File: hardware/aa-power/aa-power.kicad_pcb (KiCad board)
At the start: 4 copper layers, 175.3 x 96.5 mm, 172 parts, among them CN1 Barrel_Jack, CN10 6P6C, CN11 6P6C, CN12 6P6C, CN13 6P6C, CN14 Conn_01x08, CN15 Conn_01x08, CN16 Conn_01x08, CN17 8P8C, CN18 8P8C, CN19 8P8C, CN2 Conn_01x02, CN20 Conn_01x02, CN21 Conn_01x02, CN22 Conn_01x02, CN23 Conn_01x02, CN24 Conn_01x02, CN25 Conn_01x02, CN3 Conn_01x06, CN4 Conn_01x06, CN5 6P6C, CN6 Conn_01x04, CN7 Conn_01x04, CN8 Conn_01x04, CN9 Conn_01x04, Q1 TN1610H, U1 24LC08, U2 NIS5132xx, U3 uA7805, U4 75ALS192, U5 75ALS192, U6 75ALS192, U7 75ALS192, U8 75ALS192

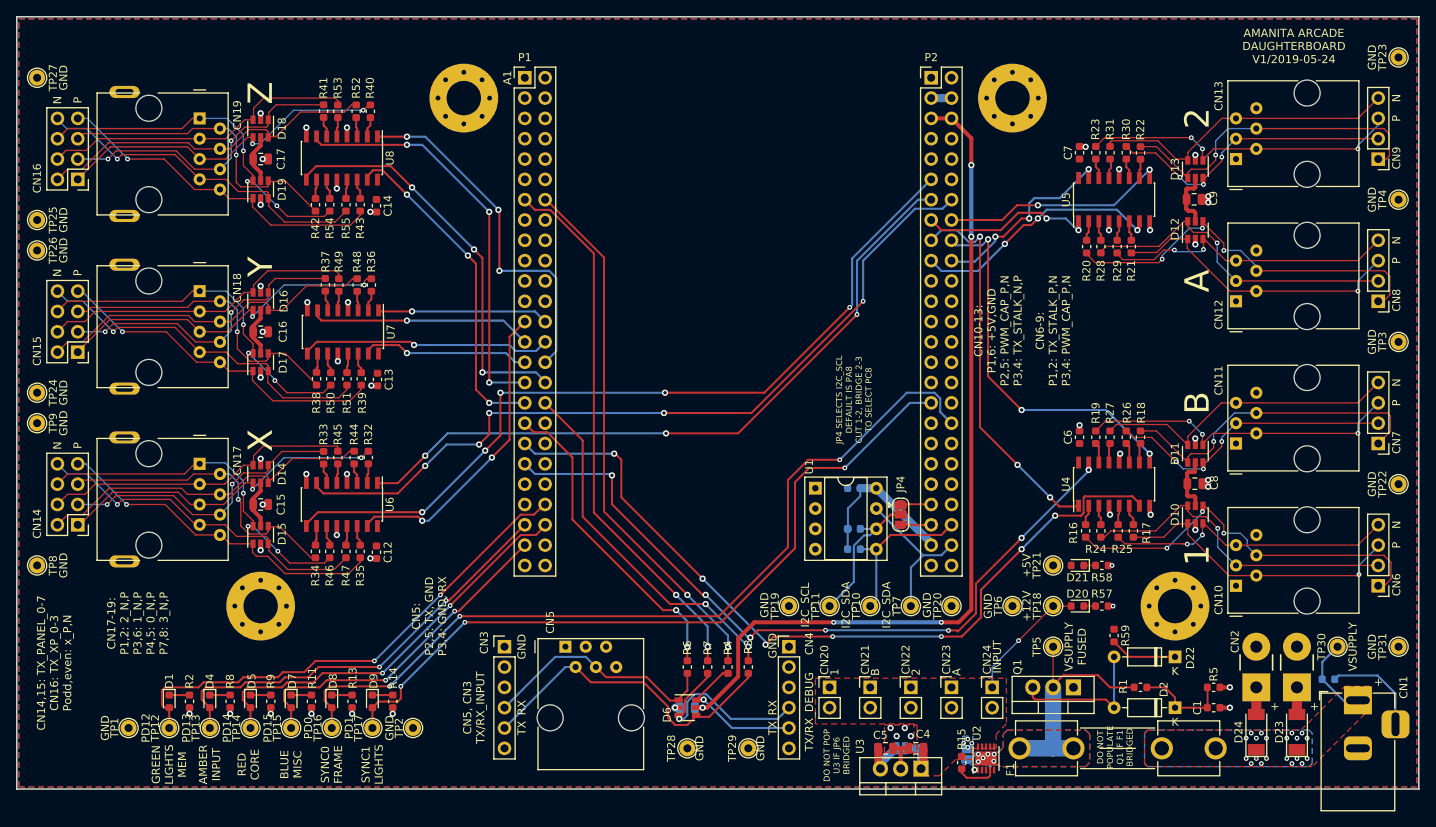
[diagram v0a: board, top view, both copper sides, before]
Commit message: Design, lay out power protection/distribution board
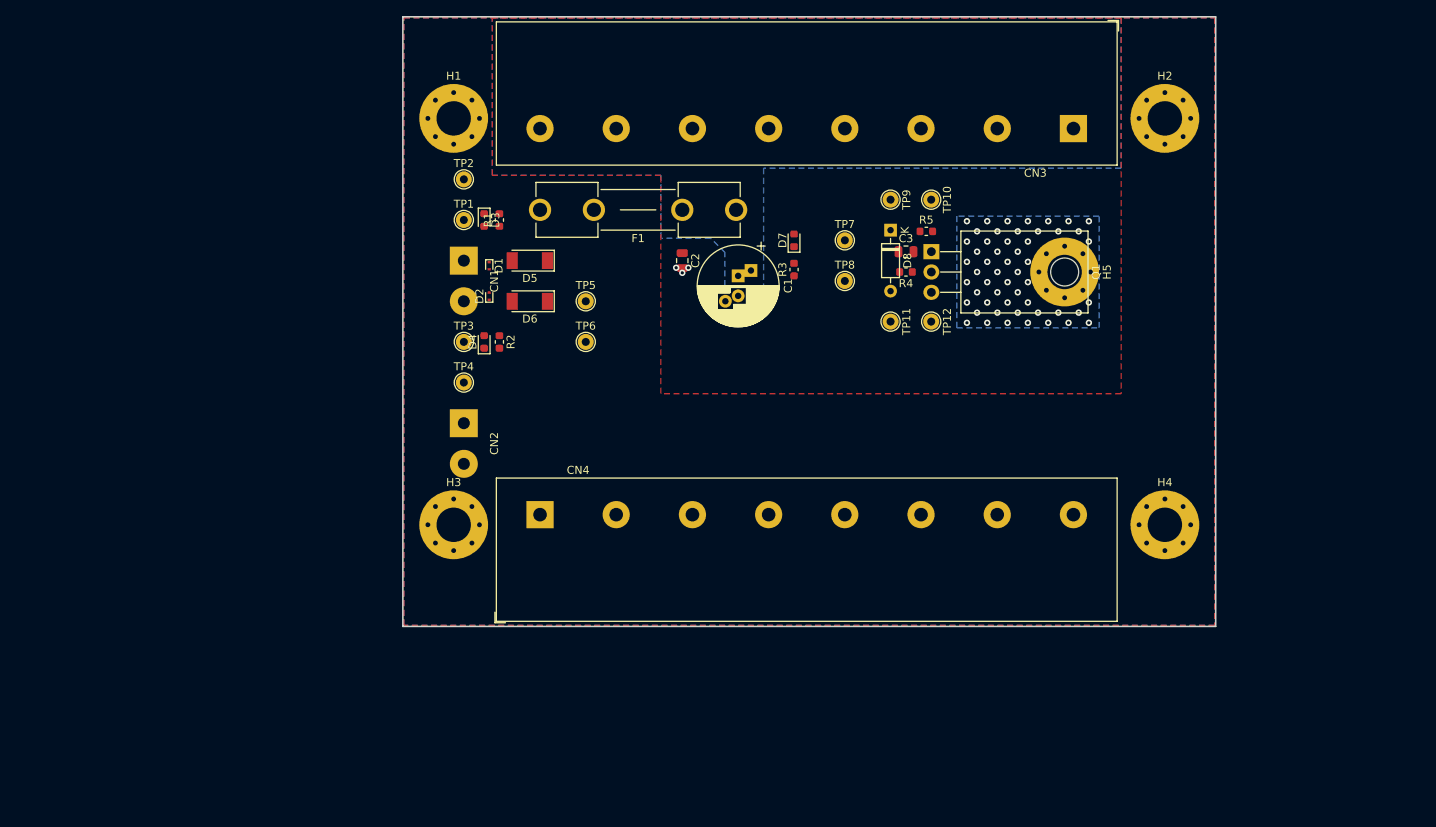
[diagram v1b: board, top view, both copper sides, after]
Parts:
- removed A1: STM32F407_Discovery_P1_P2, aa-power:STM32F407_Discovery_P1_P2_Socket
- removed C12, C13, C14, C6, C7: 0.1u, Capacitor_SMD:C_0603_1608Metric
- removed C15, C16, C17, C8, C9: 1u, Capacitor_SMD:C_0805_2012Metric
- removed C4, C5: 10u, Capacitor_SMD:C_0805_2012Metric
- removed CN10, CN11, CN12, CN13, CN5: 6P6C, aa-power:6P6C_Assmann_A-2014-1-4
- removed CN14, CN15, CN16: Conn_01x08, Connector_PinHeader_2.54mm:PinHeader_2x04_P2.54mm_Vertical
- removed CN17, CN18, CN19: 8P8C, aa-power:8P8C_Assmann_A-2014-2S-4
- removed CN20, CN21, CN22, CN23, CN24: Conn_01x02, Connector_PinHeader_2.54mm:PinHeader_1x02_P2.54mm_Vertical
- removed CN25: Conn_01x02, Connector_Wire:SolderWirePad_1x02_P5.08mm_Drill1.5mm
- removed CN6, CN7, CN8, CN9: Conn_01x04, Connector_PinHeader_2.54mm:PinHeader_1x04_P2.54mm_Vertical
- removed D10, D11, D12, D13, D14, D15, D16, D17, D18, D19: D5V0P4UR6SO, Package_TO_SOT_SMD:SOT-23-6
- removed D20, D21, D9: LED, LED_SMD:LED_0603_1608Metric
- removed D22: BZX79C5V1, Diode_THT:D_DO-35_SOD27_P7.62mm_Horizontal
- removed D23, D24: D_Schottky, aa-power:D_SOD-128
- removed JP4: SolderJumper_3_Bridged12, Jumper:SolderJumper-3_P1.3mm_Bridged2Bar12_RoundedPad1.0x1.5mm
- removed JP5, JP7: SolderJumper_2_Open, Jumper:SolderJumper-2_P1.3mm_Open_RoundedPad1.0x1.5mm
- removed R10, R12, R56: 10k, Resistor_SMD:R_0603_1608Metric
- removed R11, R13, R14, R59, R8, R9: 220, Resistor_SMD:R_0603_1608Metric
- removed R15: 33, Resistor_SMD:R_0603_1608Metric
- removed R16, R17, R18, R19, R20, R21, R22, R23, R24, R25, R26, R27, R28, R29, R30, R31, R32, R33, R34, R35, R36, R37, R38, R39, R40, R41, R42, R43, R44, R45, R46, R47, R48, R49, R50, R51, R52, R53, R54, R55: 56, Resistor_SMD:R_0603_1608Metric
- removed R57: 2.2k, Resistor_SMD:R_0603_1608Metric
- removed R58: 680, Resistor_SMD:R_0603_1608Metric
- removed R6, R7: 1k, Resistor_SMD:R_0603_1608Metric
- removed TP13, TP14, TP15, TP16, TP17, TP18, TP19, TP20, TP21, TP22, TP23, TP24, TP25, TP26, TP27, TP28, TP29, TP30, TP31: TestPoint, TestPoint:TestPoint_THTPad_D2.0mm_Drill1.0mm
- removed U1: 24LC08, Package_DIP:DIP-8_W7.62mm_Socket
- removed U2: NIS5132xx, Package_DFN_QFN:DFN-10-1EP_3x3mm_P0.5mm_EP1.75x2.7mm
- removed U3: uA7805, Package_TO_SOT_THT:TO-220-3_Vertical
- removed U4, U5, U6, U7, U8: 75ALS192, Package_SO:SOIC-16_3.9x9.9mm_P1.27mm
- added H5: MountingHole_Pad, MountingHole:MountingHole_4.3mm_M4_Pad_Via, F.Cu at (184.3, 82.7)
- C1: value 10n -> 100u; footprint Capacitor_SMD:C_0603_1608Metric -> Capacitor_THT:CP_Radial_D10.0mm_P2.50mm_P5.00mm
- C2: moved to F.Cu
- C3: value 0.1u -> 1u; footprint Capacitor_SMD:C_0603_1608Metric -> Capacitor_SMD:C_0805_2012Metric; moved to F.Cu
- CN1: value Barrel_Jack -> 12V_IN; footprint Connector_BarrelJack:BarrelJack_Horizontal -> Connector_Wire:SolderWirePad_1x02_P5.08mm_Drill1.5mm
- CN2: value Conn_01x02 -> GND_IN
- CN3: value Conn_01x06 -> 12V_OUT; footprint Connector_PinHeader_2.54mm:PinHeader_1x06_P2.54mm_Vertical -> aa-shared:TerminalBlock_OST_OSTYK44108030
- CN4: value Conn_01x06 -> GND_OUT; footprint Connector_PinHeader_2.54mm:PinHeader_1x06_P2.54mm_Vertical -> aa-shared:TerminalBlock_OST_OSTYK44108030
- D1: value LED -> DF2S16FS; footprint LED_SMD:LED_0603_1608Metric -> aa-shared:D_SOD-923
- D2: value BZX79C15 -> DF2S16FS; footprint Diode_THT:D_DO-35_SOD27_P7.62mm_Horizontal -> aa-shared:D_SOD-923
- D3: value DF2S16FS -> LED; footprint aa-power:D_SOD-923 -> LED_SMD:LED_0603_1608Metric; moved to F.Cu
- D5: value LED -> D_Schottky; footprint LED_SMD:LED_0603_1608Metric -> aa-shared:D_SOD-128
- D6: value D5V0P4UR6SO -> D_Schottky; footprint Package_TO_SOT_SMD:SOT-23-6 -> aa-shared:D_SOD-128
- D8: value LED -> BZX79C15; footprint LED_SMD:LED_0603_1608Metric -> Diode_THT:D_DO-35_SOD27_P7.62mm_Horizontal
- F1: footprint aa-power:Fuseholder_Clip_5x20_Bel_FC-211-22 -> aa-shared:Fuseholder_Clip_5x20_Bel_FC-211-22
- Q1: footprint Package_TO_SOT_THT:TO-220-3_Vertical -> Package_TO_SOT_THT:TO-220-3_Horizontal_TabDown
- R1, R2: value 220 -> 2.2k
- R3: value 120 -> 2.2k
- R4: value 120 -> 470
- TP1: value TestPoint -> 12V_IN_A
- TP10, TP12, TP2, TP4, TP5, TP6, TP8: value TestPoint -> GND
- TP11: value TestPoint -> 12V_IN
- TP3: value TestPoint -> 12V_IN_B
- moved CN1 124.5 mm to (109.2, 81.3), turned to 270 degrees
- moved TP4 119.1 mm to (109.2, 96.5), turned to 0 degrees
- moved TP3 116.8 mm to (109.2, 91.4), turned to 0 degrees
- moved TP9 110.3 mm to (162.6, 73.7)
- moved TP12 107.9 mm to (167.6, 88.9), turned to 270 degrees
- moved TP8 107.0 mm to (156.8, 83.8), turned to 0 degrees
- moved CN2 104.4 mm to (109.2, 101.6), turned to 270 degrees
- moved D2 100.0 mm to (112.4, 85.7), turned to 90 degrees
- moved R1 99.2 mm to (113.7, 76.2), turned to 90 degrees
- moved CN3 96.2 mm to (185.4, 64.8), turned to 180 degrees
- moved D3 92.7 mm to (111.8, 76.2)
- moved D8 91.4 mm to (162.6, 77.5)
- moved H3 90.7 mm to (108.0, 114.3), turned to 0 degrees
- moved H2 87.7 mm to (196.8, 63.5), turned to 0 degrees
- moved D7 85.3 mm to (150.5, 78.7), turned to 90 degrees
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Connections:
- C1 pad 1: Net-(C1-Pad1) -> /Q1_TAB
- C2 pad 1: +3V -> /Q1_TAB
- C3 pad 1: /MEM_PWR -> Net-(C3-Pad1)
- CN1 pad 2: GND -> Net-(CN1-Pad2)
- CN2 pad 1: Net-(CN2-Pad1) -> GND
- CN3 pad 1: GND -> /Q1_TAB
- CN3 pad 2: Net-(CN3-Pad2) -> /Q1_TAB
- CN3 pad 3: Net-(CN3-Pad3) -> /Q1_TAB
- CN3 pad 4: /RX_INPUT_S -> /Q1_TAB
- CN3 pad 5: /TX_INPUT_S -> /Q1_TAB
- CN3 pad 6: Net-(CN3-Pad6) -> /Q1_TAB
- CN4 pad 2: Net-(CN4-Pad2) -> GND
- CN4 pad 3: Net-(CN4-Pad3) -> GND
- CN4 pad 4: /RX_DEBUG_S -> GND
- CN4 pad 5: /TX_DEBUG_S -> GND
- CN4 pad 6: Net-(CN4-Pad6) -> GND
- D1 pad 1: Net-(D1-Pad1) -> Net-(CN1-Pad1)
- D1 pad 2: /DB_GREEN -> GND
- D2 pad 1: Net-(C1-Pad1) -> Net-(CN1-Pad2)
- D2 pad 2: Net-(D2-Pad2) -> GND
- D3 pad 2: GND -> Net-(CN1-Pad1)
- D4 pad 2: /DB_ORANGE -> Net-(CN1-Pad2)
- D5 pad 2: /DB_RED -> Net-(CN1-Pad1)
- D6 pad 1: /RX_INPUT_S -> Net-(D5-Pad1)
- D6 pad 2: GND -> Net-(CN1-Pad2)
- D7 pad 2: /DB_BLUE -> /Q1_TAB
- D8 pad 1: Net-(D8-Pad1) -> Net-(C3-Pad1)
- D8 pad 2: /DB_SYNC_0 -> Net-(D8-Pad2)
- F1 pad 1: Net-(D3-Pad1) -> /Q1_TAB
- F1 pad 2: Net-(CN1-Pad1) -> Net-(D5-Pad1)
- Q1 pad 2: Net-(D3-Pad1) -> /Q1_TAB
- Q1 pad 3: Net-(D2-Pad2) -> Net-(D8-Pad2)
- R1 pad 1: Net-(D3-Pad1) -> GND
- R1 pad 2: Net-(C1-Pad1) -> Net-(D3-Pad1)
- R2 pad 2: Net-(D1-Pad1) -> Net-(D4-Pad1)
- R3 pad 1: /TX_INPUT -> GND
- R3 pad 2: /TX_INPUT_S -> Net-(D7-Pad1)
- R4 pad 1: /TX_DEBUG -> /Q1_TAB
- R4 pad 2: /TX_DEBUG_S -> Net-(C3-Pad1)
- R5 pad 1: Net-(C1-Pad1) -> Net-(C3-Pad1)
- TP1 pad 1: GND -> Net-(CN1-Pad1)
- TP10 pad 1: /I2C_SDA -> GND
- TP11 pad 1: /I2C_SCL -> Net-(D8-Pad2)
- TP12 pad 1: /DB_GREEN -> GND
- TP3 pad 1: GND -> Net-(CN1-Pad2)
- TP5 pad 1: Net-(D3-Pad1) -> Net-(D5-Pad1)
- TP7 pad 1: /MEM_WP -> /Q1_TAB
- TP9 pad 1: GND -> Net-(C3-Pad1)
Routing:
- net +3V: track 108.1 -> 0.00 mm, vias 5 -> 0
- net /DB_SYNC_0: track 106.4 -> 0.00 mm, vias 3 -> 0
- net /TX_PANEL_2: track 103.1 -> 0.00 mm, vias 5 -> 0
- net /PWM_CAP_1: track 101.7 -> 0.00 mm, vias 7 -> 0
- net /TX_PANEL_1: track 99.9 -> 0.00 mm, vias 5 -> 0
- net /DB_SYNC_1: track 93.9 -> 0.00 mm, vias 3 -> 0
- net /PWM_CAP_B: track 93.5 -> 0.00 mm, vias 7 -> 0
- net /TX_PANEL_0: track 88.0 -> 0.00 mm, vias 3 -> 0
- net /RX_DEBUG: track 68.2 -> 0.00 mm, vias 2 -> 0
- net /TX_DEBUG: track 67.2 -> 0.00 mm, vias 2 -> 0
- net /DB_GREEN: track 63.0 -> 0.00 mm, vias 2 -> 0
- net /DB_ORANGE: track 54.5 -> 0.00 mm, vias 2 -> 0
- net /TX_XP_1: track 51.5 -> 0.00 mm, vias 3 -> 0
- net /DB_RED: track 51.5 -> 0.00 mm, vias 2 -> 0
- net /TX_XP_2: track 50.3 -> 0.00 mm, vias 3 -> 0
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- added copper zone on B.Cu, net /Q1_TAB
- added copper zone on F.Cu, net /Q1_TAB
- removed copper zone on F.Cu, net +5V
- removed copper zone on B.Cu, net Net-(CN1-Pad1)
- removed copper zone on F.Cu, net Net-(CN1-Pad1)
- removed copper zone on B.Cu, net Net-(D3-Pad1)
- removed copper zone on F.Cu, net Net-(D3-Pad1)
- removed copper zone on B.Cu, net VDD
- removed copper zone on F.Cu, net VDD
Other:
- board size 175.3 x 96.5 mm -> 101.6 x 76.2 mm
- copper layers 4 -> 2
- net class Default: clearance 0.1524 -> 0.254; via_dia 0.7874 -> 0.8; via_drill 0.4064 -> 0.4
- net class High Current removed
- net class Line Drive Broadside removed
- net class Line Drive Microstrip removed
- net class Power removed
- rule pad_to_mask_clearance: 0.051 -> 0
- rule trace_clearance: 0.1524 -> 0.254
- board text removed: "+"
- board text removed: "+12V"
- board text removed: "+5V"
- board text removed: "1"
- board text removed: "2"
- board text removed: "A"
- board text removed: "AMANITA ARCADE DAUGHTERBOARD V1/2019-05-24"
- board text removed: "AMBER INPUT"
- board text removed: "B"
- board text removed: "BLUE MISC"
- board text removed: "BRIDGE JP5 IF U2 NOT POPULATED"
- board text removed: "BRIDGE JP6 TO USE +5V FROM STM32F4 DISCOVERY BOARD A1 DO NOT POPULATE U3"
- board text removed: "BRIDGE JP7 TO CONNECT VDD AND +5V POWER INPUT MUST BE REGULATED DO NOT POPULATE U3"
- board text removed: "CN10-13: P1,6: +5V,GND P2,5: PWM_CAP_P,N P3,4: TX_STALK_N,P"
- board text removed: "CN14,15: TX_PANEL_0-7 CN16: TX_XP_0-3 Podd,even: x_P,N"
- board text removed: "CN17-19: P1,2: 2_N,P P3,6: 1_N,P P4,5: 0_N,P P7,8: 3_N,P"
- board text removed: "CN5, CN3 TX/RX_INPUT"
- board text removed: "CN5: P2,5: TX, GND P3,4: GND, RX"
- board text removed: "CN6-9: P1,2: TX_STALK_P,N P3,4: PWM_CAP_P,N"
- board text removed: "CUT JP1 IF STM32F4 DISCOVERY BOARD A1 IS INDEPENDENTLY POWERED"
- board text removed: "DO NOT POP U3 IF JP6 BRIDGED"
- board text removed: "DO NOT POPULATE Q1 IF F1 BRIDGED"
- board text removed: "GND"
- board text removed: "GREEN LIGHTS MEM"
- board text removed: "I2C_SCL"
- board text removed: "I2C_SDA"
- board text removed: "INPUT"
- board text removed: "JP4 SELECTS I2C_SCL DEFAULT IS PA8 CUT 1-2, BRIDGE 2-3 TO SELECT PC8"
- board text removed: "N"
- board text removed: "P"
- board text removed: "PD0"
- board text removed: "PD1"
- board text removed: "PD12"
- board text removed: "PD13"
- board text removed: "PD14"
- board text removed: "PD15"
- board text removed: "R56 CONNECTS VSUPPLY AND GND WHEN CN1 UNPLUGGED"
- board text removed: "RED CORE"
- board text removed: "RX"
- board text removed: "SYNC0 FRAME"
- board text removed: "SYNC1 LIGHTS"
- board text removed: "TX"
- board text removed: "TX/RX_DEBUG"
- board text removed: "VSUPPLY"
- board text removed: "VSUPPLY FUSED"
- board text removed: "X"
- board text removed: "Y"
- board text removed: "Z"

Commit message: Substantial rework of system, new layouts done for daughterboard, power, stalk receiver
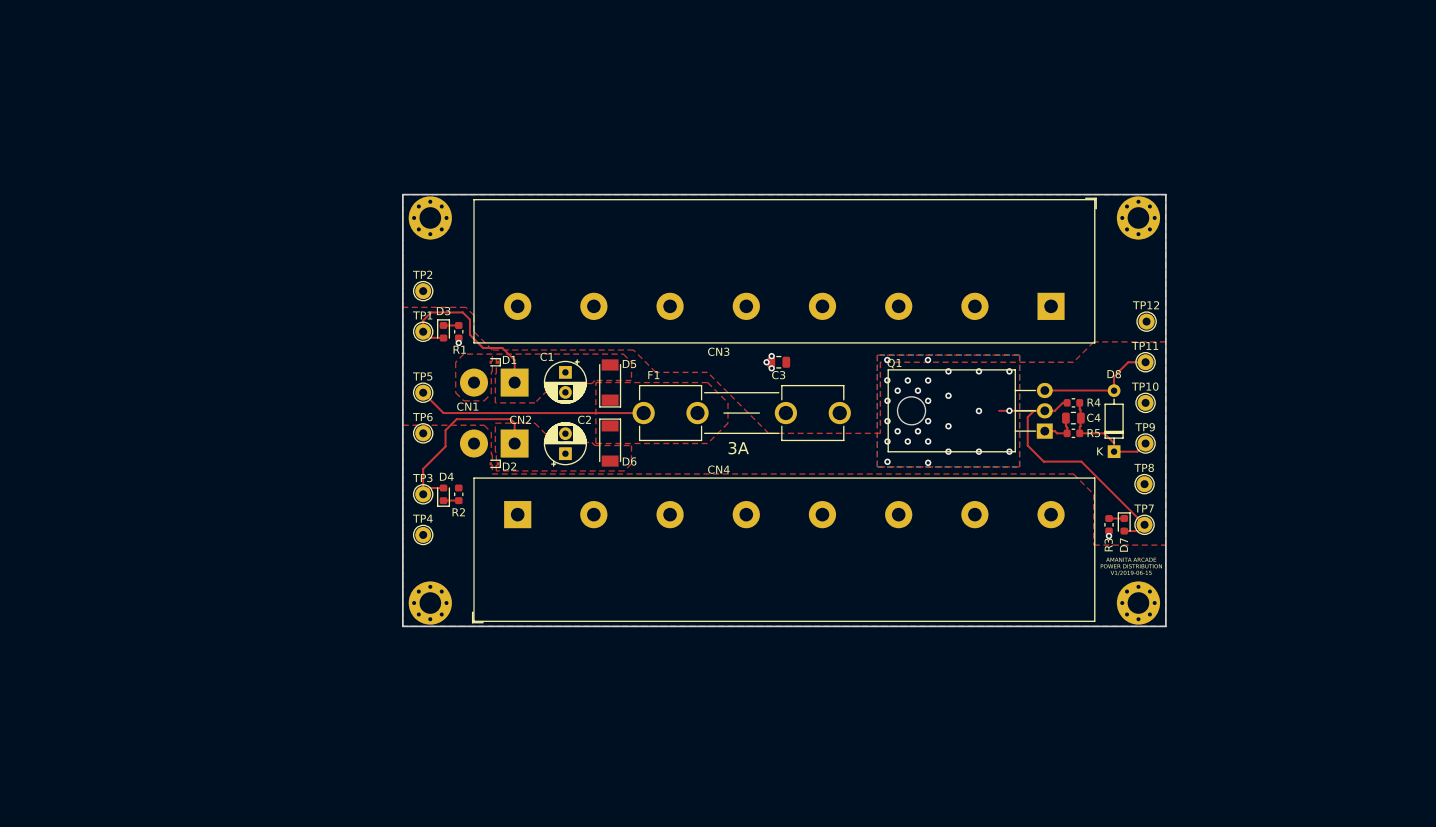
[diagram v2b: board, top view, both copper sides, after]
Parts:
- removed H5: MountingHole_Pad, MountingHole:MountingHole_4.3mm_M4_Pad_Via
- added C4: 1u, Capacitor_SMD:C_0805_2012Metric, F.Cu at (185.4, 101.0)
- C1: value 100u -> 10u; footprint Capacitor_THT:CP_Radial_D10.0mm_P2.50mm_P5.00mm -> Capacitor_THT:CP_Radial_D5.0mm_P2.50mm
- C2: value 1u -> 10u; footprint Capacitor_SMD:C_0805_2012Metric -> Capacitor_THT:CP_Radial_D5.0mm_P2.50mm
- CN1: value 12V_IN -> VIN_A
- CN2: value GND_IN -> VIN_B
- H1, H2, H3, H4: footprint MountingHole:MountingHole_4.3mm_M4_Pad_Via -> MountingHole:MountingHole_2.7mm_M2.5_Pad_Via
- moved H2 92.7 mm to (105.0, 75.9)
- moved H1 86.5 mm to (193.5, 75.9)
- moved D7 54.5 mm to (191.8, 114.3), turned to 270 degrees
- moved TP7 51.7 mm to (194.3, 114.3)
- moved R3 50.7 mm to (189.9, 114.3)
- moved TP8 45.3 mm to (194.3, 109.2)
- moved TP9 44.1 mm to (194.4, 104.1), turned to 0 degrees
- moved D8 39.3 mm to (190.5, 105.2), turned to 90 degrees
- moved TP10 36.9 mm to (194.4, 99.1), turned to 0 degrees
- moved TP11 32.3 mm to (194.4, 94.0), turned to 0 degrees
- moved R5 31.2 mm to (185.4, 102.9), turned to 180 degrees
- moved F1 28.5 mm to (156.2, 100.3)
- moved C2 28.2 mm to (121.9, 105.4), turned to 90 degrees
- moved TP12 26.9 mm to (194.6, 88.9), turned to 0 degrees
- moved R4 26.6 mm to (185.4, 99.1), turned to 0 degrees
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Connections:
- C1 pad 1: /Q1_TAB -> Net-(C1-Pad1)
- C2 pad 1: /Q1_TAB -> Net-(C2-Pad1)
- C3 pad 1: Net-(C3-Pad1) -> /+12V
- CN1 pad 1: Net-(CN1-Pad1) -> Net-(C1-Pad1)
- CN1 pad 2: Net-(CN1-Pad2) -> GND
- CN2 pad 1: GND -> Net-(C2-Pad1)
- CN3 pad 1: /Q1_TAB -> /+12V
- CN3 pad 2: /Q1_TAB -> /+12V
- CN3 pad 3: /Q1_TAB -> /+12V
- CN3 pad 4: /Q1_TAB -> /+12V
- CN3 pad 5: /Q1_TAB -> /+12V
- CN3 pad 6: /Q1_TAB -> /+12V
- CN3 pad 7: /Q1_TAB -> /+12V
- CN3 pad 8: /Q1_TAB -> /+12V
- D1 pad 1: Net-(CN1-Pad1) -> Net-(C1-Pad1)
- D2 pad 1: Net-(CN1-Pad2) -> Net-(C2-Pad1)
- D3 pad 2: Net-(CN1-Pad1) -> Net-(C1-Pad1)
- D4 pad 2: Net-(CN1-Pad2) -> Net-(C2-Pad1)
- D5 pad 2: Net-(CN1-Pad1) -> Net-(C1-Pad1)
- D6 pad 2: Net-(CN1-Pad2) -> Net-(C2-Pad1)
- D7 pad 2: /Q1_TAB -> /+12V
- D8 pad 1: Net-(C3-Pad1) -> Net-(C4-Pad1)
- F1 pad 1: /Q1_TAB -> /+12V
- Q1 pad 2: /Q1_TAB -> /+12V
- R4 pad 1: /Q1_TAB -> /+12V
- R4 pad 2: Net-(C3-Pad1) -> Net-(C4-Pad1)
- R5 pad 1: Net-(C3-Pad1) -> Net-(C4-Pad1)
- TP1 pad 1: Net-(CN1-Pad1) -> Net-(C1-Pad1)
- TP3 pad 1: Net-(CN1-Pad2) -> Net-(C2-Pad1)
- TP7 pad 1: /Q1_TAB -> /+12V
- TP9 pad 1: Net-(C3-Pad1) -> Net-(C4-Pad1)
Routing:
- net /+12V: track 0.00 -> 36.4 mm, vias 0 -> 28
- net Net-(D5-Pad1): track 0.00 -> 28.6 mm
- net Net-(C2-Pad1): track 0.00 -> 24.0 mm
- net Net-(C1-Pad1): track 0.00 -> 22.6 mm
- net Net-(D8-Pad2): track 0.00 -> 15.1 mm
- net Net-(C4-Pad1): track 0.00 -> 14.1 mm
- net GND: track 2.15 -> 8.28 mm, vias 3 -> 5
- net Net-(D7-Pad1): track 0.00 -> 2.04 mm
- net Net-(D4-Pad1): track 0.00 -> 1.92 mm
- net Net-(D3-Pad1): track 0.00 -> 1.92 mm
- net /Q1_TAB: vias 53 -> 0
- added copper zone on B.Cu, net /+12V
- added copper zone on F.Cu, net /+12V
- added copper zone on F.Cu, net Net-(C1-Pad1)
- added copper zone on F.Cu, net Net-(C2-Pad1)
- added copper zone on F.Cu, net Net-(D5-Pad1)
- removed copper zone on B.Cu, net /Q1_TAB
- removed copper zone on F.Cu, net /Q1_TAB
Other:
- board size 101.6 x 76.2 mm -> 95.4 x 54 mm
- board text added: "3A"
- board text added: "AMANITA ARCADE POWER DISTRIBUTION V1/2019-06-15"

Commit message: Final designs and actual sent gerbers for first for-real run
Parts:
- added FD1: Fiducial, Fiducial:Fiducial_1mm_Dia_2.54mm_Outer_CopperTop, F.Cu at (106.7, 119.4)
- added FD2: Fiducial, Fiducial:Fiducial_1mm_Dia_2.54mm_Outer_CopperTop, F.Cu at (191.8, 81.3)
- added FD5: Fiducial, aa-shared:StencilAlignment_1.27mm, F.Cu at (104.1, 119.4)
- added FD6: Fiducial, aa-shared:StencilAlignment_1.27mm, F.Cu at (194.3, 81.3)
- D5, D6: value D_Schottky -> TSS83L45
- D8: footprint Diode_THT:D_DO-35_SOD27_P7.62mm_Horizontal -> Diode_THT:D_DO-35_SOD27_P2.54mm_Vertical_KathodeUp
- TP1: value 12V_IN_A -> +12V_IN_A; footprint TestPoint:TestPoint_THTPad_D2.0mm_Drill1.0mm -> aa-shared:TestPoint_Loop_D1.80mm_Drill1.0mm_Beaded
- TP10, TP12, TP2, TP4, TP6, TP8: footprint TestPoint:TestPoint_THTPad_D2.0mm_Drill1.0mm -> aa-shared:TestPoint_Loop_D1.80mm_Drill1.0mm_Beaded
- TP11: value 12V_IN -> OV_TRIG; footprint TestPoint:TestPoint_THTPad_D2.0mm_Drill1.0mm -> aa-shared:TestPoint_Loop_D1.80mm_Drill1.0mm_Beaded
- TP3: value 12V_IN_B -> +12V_IN_B; footprint TestPoint:TestPoint_THTPad_D2.0mm_Drill1.0mm -> aa-shared:TestPoint_Loop_D1.80mm_Drill1.0mm_Beaded
- TP5: value GND -> +12V_UNFS; footprint TestPoint:TestPoint_THTPad_D2.0mm_Drill1.0mm -> aa-shared:TestPoint_Loop_D1.80mm_Drill1.0mm_Beaded
- TP7: value TestPoint -> +12V; footprint TestPoint:TestPoint_THTPad_D2.0mm_Drill1.0mm -> aa-shared:TestPoint_Loop_D1.80mm_Drill1.0mm_Beaded
- TP9: value TestPoint -> OV_Z; footprint TestPoint:TestPoint_THTPad_D2.0mm_Drill1.0mm -> aa-shared:TestPoint_Loop_D1.80mm_Drill1.0mm_Beaded
- moved D8 8.97 mm to (188.1, 96.5), turned to 180 degrees
- moved R1 5.08 mm to (108.7, 85.1), turned to 270 degrees
- moved R2 5.08 mm to (108.6, 115.6), turned to 90 degrees
- moved R3 5.08 mm to (189.9, 109.2), turned to 270 degrees
- moved D3 2.03 mm to (108.7, 90.2)
- moved D7 1.91 mm to (189.9, 114.3)
- moved D4 1.90 mm to (108.6, 110.5)
- turned TP1 to 90 degrees
- turned TP10 to 270 degrees
- turned TP11 to 270 degrees
- turned TP12 to 270 degrees
- turned TP2 to 90 degrees
- turned TP3 to 90 degrees
- turned TP4 to 90 degrees
- turned TP5 to 90 degrees
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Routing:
- net Net-(C1-Pad1): track 22.6 -> 15.8 mm
- net Net-(C4-Pad1): track 14.1 -> 16.2 mm
- net Net-(C2-Pad1): track 24.0 -> 25.9 mm
- net Net-(D3-Pad1): track 1.92 -> 3.57 mm
- net Net-(D4-Pad1): track 1.92 -> 3.53 mm
- net Net-(D7-Pad1): track 2.04 -> 3.53 mm
